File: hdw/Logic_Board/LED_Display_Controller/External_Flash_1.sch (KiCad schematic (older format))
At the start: 16 parts, among them U1801 SST25PF020B

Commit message: Added some digikey partnumbers to components
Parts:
- C1801: footprint (none) -> Capacitors_SMD:C_0603; Digi-Key PN PN -> 311-1344-1-ND; Voltage 25V -> 50V
- C1802: Digi-Key PN PN -> 1276-1921-1-ND; Voltage 25V -> 50V
- C1803: Digi-Key PN PN -> 1276-1018-1-ND; Voltage 25V -> 50V
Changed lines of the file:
@@
 F 0 "C1801" H 5815 5530 50  0000 L CNN
 F 1 "0.1uF" H 5815 5330 50  0000 L CNN
-F 2 "" H 5828 5280 50  0001 C CNN
+F 2 "Capacitors_SMD:C_0603" H 5828 5280 50  0001 C CNN
 F 3 "" H 5815 5530 50  0001 C CNN
 F 4 "0603" H 5640 5530 50  0000 R CNN "display_footprint"
-F 5 "25V" H 5640 5430 50  0000 R CNN "Voltage"
+F 5 "50V" H 5640 5430 50  0000 R CNN "Voltage"
 F 6 "X7R" H 5640 5330 50  0000 R CNN "Dielectric"
-F 7 "PN" H 6215 5930 60  0001 C CNN "Digi-Key PN"
+F 7 "311-1344-1-ND" H 6215 5930 60  0001 C CNN "Digi-Key PN"
 	1    5790 5430
 	1    0    0    -1
@@
 F 3 "" H 6115 5530 50  0001 C CNN
 F 4 "0603" H 5940 5530 50  0001 R CNN "display_footprint"
-F 5 "25V" H 5940 5430 50  0001 R CNN "Voltage"
+F 5 "50V" H 5940 5430 50  0001 R CNN "Voltage"
 F 6 "X7R" H 5940 5330 50  0001 R CNN "Dielectric"
-F 7 "PN" H 6515 5930 60  0001 C CNN "Digi-Key PN"
+F 7 "1276-1921-1-ND" H 6515 5930 60  0001 C CNN "Digi-Key PN"
 	1    6090 5430
 	1    0    0    -1
@@
 F 3 "" H 6415 5530 50  0001 C CNN
 F 4 "0603" H 6240 5530 50  0001 R CNN "display_footprint"
-F 5 "25V" H 6240 5430 50  0001 R CNN "Voltage"
+F 5 "50V" H 6240 5430 50  0001 R CNN "Voltage"
 F 6 "X7R" H 6240 5330 50  0001 R CNN "Dielectric"
-F 7 "PN" H 6815 5930 60  0001 C CNN "Digi-Key PN"
+F 7 "1276-1018-1-ND" H 6815 5930 60  0001 C CNN "Digi-Key PN"
 	1    6390 5430
 	1    0    0    -1

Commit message: Finished first pass of digikey part numbers
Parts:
- R1801, R1802, R1803, R1804, R1805, R1812: Digi-Key PN PN -> A106047CT-ND
- R1806, R1807, R1808, R1809, R1810, R1811: Digi-Key PN PN -> RMCF0603FT10K0CT-ND
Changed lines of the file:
@@
 F 5 "1%" H 5410 4320 50  0000 L CNN "Tolerance"
 F 6 "1/10W" H 5410 4240 50  0000 L CNN "Wattage"
-F 7 "PN" H 5630 4720 60  0001 C CNN "Digi-Key PN"
+F 7 "RMCF0603FT10K0CT-ND" H 5630 4720 60  0001 C CNN "Digi-Key PN"
 	1    5330 4320
 	1    0    0    -1
@@
 F 5 "1%" H 4600 4320 50  0000 L CNN "Tolerance"
 F 6 "1/10W" H 4600 4240 50  0000 L CNN "Wattage"
-F 7 "PN" H 4820 4720 60  0001 C CNN "Digi-Key PN"
+F 7 "RMCF0603FT10K0CT-ND" H 4820 4720 60  0001 C CNN "Digi-Key PN"
 	1    4520 4320
 	1    0    0    -1
@@
 F 5 "1%" H 5190 3130 50  0000 L CNN "Tolerance"
 F 6 "1/10W" H 5190 3050 50  0000 L CNN "Wattage"
-F 7 "PN" H 5410 3530 60  0001 C CNN "Digi-Key PN"
+F 7 "RMCF0603FT10K0CT-ND" H 5410 3530 60  0001 C CNN "Digi-Key PN"
 	1    5110 3130
 	1    0    0    -1
@@
 F 5 "1%" H 4600 3130 50  0000 L CNN "Tolerance"
 F 6 "1/10W" H 4600 3050 50  0000 L CNN "Wattage"
-F 7 "PN" H 4820 3530 60  0001 C CNN "Digi-Key PN"
+F 7 "RMCF0603FT10K0CT-ND" H 4820 3530 60  0001 C CNN "Digi-Key PN"
 	1    4520 3130
 	1    0    0    -1
@@
 F 5 "1%" H 4010 3130 50  0000 L CNN "Tolerance"
 F 6 "1/10W" H 4010 3050 50  0000 L CNN "Wattage"
-F 7 "PN" H 4230 3530 60  0001 C CNN "Digi-Key PN"
+F 7 "RMCF0603FT10K0CT-ND" H 4230 3530 60  0001 C CNN "Digi-Key PN"
 	1    3930 3130
 	1    0    0    -1
@@
 F 5 "1%" H 6830 3850 50  0000 L CNN "Tolerance"
 F 6 "1/10W" H 6830 3770 50  0000 L CNN "Wattage"
-F 7 "PN" H 7050 4250 60  0001 C CNN "Digi-Key PN"
+F 7 "RMCF0603FT10K0CT-ND" H 7050 4250 60  0001 C CNN "Digi-Key PN"
 	1    6750 3850
 	1    0    0    -1
@@
 F 5 "1%" V 3620 3450 50  0001 C CNN "Tolerance"
 F 6 "1/10W" V 3720 3450 50  0001 C CNN "Wattage"
-F 7 "PN" H 3720 3850 60  0001 C CNN "Digi-Key PN"
+F 7 "A106047CT-ND" H 3720 3850 60  0001 C CNN "Digi-Key PN"
 	1    3420 3450
 	0    1    1    0
@@
 F 5 "1%" V 7330 3450 50  0001 C CNN "Tolerance"
 F 6 "1/10W" V 7430 3450 50  0001 C CNN "Wattage"
-F 7 "PN" H 7430 3850 60  0001 C CNN "Digi-Key PN"
+F 7 "A106047CT-ND" H 7430 3850 60  0001 C CNN "Digi-Key PN"
 	1    7130 3450
 	0    1    1    0
@@
 F 5 "1%" V 3620 3550 50  0001 C CNN "Tolerance"
 F 6 "1/10W" V 3720 3550 50  0001 C CNN "Wattage"
-F 7 "PN" H 3720 3950 60  0001 C CNN "Digi-Key PN"
+F 7 "A106047CT-ND" H 3720 3950 60  0001 C CNN "Digi-Key PN"
 	1    3420 3550
 	0    1    1    0
@@
 F 5 "1%" V 3620 3750 50  0001 C CNN "Tolerance"
 F 6 "1/10W" V 3720 3750 50  0001 C CNN "Wattage"
-F 7 "PN" H 3720 4150 60  0001 C CNN "Digi-Key PN"
+F 7 "A106047CT-ND" H 3720 4150 60  0001 C CNN "Digi-Key PN"
 	1    3420 3750
 	0    1    1    0
@@
 F 5 "1%" V 3620 3850 50  0001 C CNN "Tolerance"
 F 6 "1/10W" V 3720 3850 50  0001 C CNN "Wattage"
-F 7 "PN" H 3720 4250 60  0001 C CNN "Digi-Key PN"
+F 7 "A106047CT-ND" H 3720 4250 60  0001 C CNN "Digi-Key PN"
 	1    3420 3850
 	0    1    1    0
@@
 F 5 "1%" V 3620 3650 50  0001 C CNN "Tolerance"
 F 6 "1/10W" V 3720 3650 50  0001 C CNN "Wattage"
-F 7 "PN" H 3720 4050 60  0001 C CNN "Digi-Key PN"
+F 7 "A106047CT-ND" H 3720 4050 60  0001 C CNN "Digi-Key PN"
 	1    3420 3650
 	0    1    1    0

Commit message: First pass assignment of footprints to all components
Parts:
- C1802, C1803: footprint (none) -> Capacitors_SMD:C_0603
- R1801, R1802, R1803, R1804, R1805, R1806, R1807, R1808, R1809, R1810, R1811, R1812: footprint (none) -> Resistors_SMD:R_0603
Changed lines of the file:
@@
 F 0 "R1810" H 5270 4320 50  0000 R CNN
 F 1 "10k" V 5330 4320 50  0000 C CNN
-F 2 "" H 5330 4320 50  0001 C CNN
+F 2 "Resistors_SMD:R_0603" H 5330 4320 50  0001 C CNN
 F 3 "" H 5330 4320 50  0001 C CNN
 F 4 "0603" H 5410 4400 50  0000 L CNN "display_footprint"
@@
 F 0 "R1808" H 4460 4320 50  0000 R CNN
 F 1 "10k" V 4520 4320 50  0000 C CNN
-F 2 "" H 4520 4320 50  0001 C CNN
+F 2 "Resistors_SMD:R_0603" H 4520 4320 50  0001 C CNN
 F 3 "" H 4520 4320 50  0001 C CNN
 F 4 "0603" H 4600 4400 50  0000 L CNN "display_footprint"
@@
 F 0 "R1809" H 5050 3130 50  0000 R CNN
 F 1 "10k" V 5110 3130 50  0000 C CNN
-F 2 "" H 5110 3130 50  0001 C CNN
+F 2 "Resistors_SMD:R_0603" H 5110 3130 50  0001 C CNN
 F 3 "" H 5110 3130 50  0001 C CNN
 F 4 "0603" H 5190 3210 50  0000 L CNN "display_footprint"
@@
 F 0 "R1807" H 4460 3130 50  0000 R CNN
 F 1 "10k" V 4520 3130 50  0000 C CNN
-F 2 "" H 4520 3130 50  0001 C CNN
+F 2 "Resistors_SMD:R_0603" H 4520 3130 50  0001 C CNN
 F 3 "" H 4520 3130 50  0001 C CNN
 F 4 "0603" H 4600 3210 50  0000 L CNN "display_footprint"
@@
 F 0 "R1806" H 3870 3130 50  0000 R CNN
 F 1 "10k" V 3930 3130 50  0000 C CNN
-F 2 "" H 3930 3130 50  0001 C CNN
+F 2 "Resistors_SMD:R_0603" H 3930 3130 50  0001 C CNN
 F 3 "" H 3930 3130 50  0001 C CNN
 F 4 "0603" H 4010 3210 50  0000 L CNN "display_footprint"
@@
 F 0 "R1811" H 6690 3850 50  0000 R CNN
 F 1 "10k" V 6750 3850 50  0000 C CNN
-F 2 "" H 6750 3850 50  0001 C CNN
+F 2 "Resistors_SMD:R_0603" H 6750 3850 50  0001 C CNN
 F 3 "" H 6750 3850 50  0001 C CNN
 F 4 "0603" H 6830 3930 50  0000 L CNN "display_footprint"
@@
 F 0 "R1801" V 3380 3580 50  0000 L CNN
 F 1 "100" V 3420 3450 50  0000 C CNN
-F 2 "" H 3420 3450 50  0001 C CNN
+F 2 "Resistors_SMD:R_0603" H 3420 3450 50  0001 C CNN
 F 3 "" H 3420 3450 50  0001 C CNN
 F 4 "0603" V 3520 3450 50  0001 C CNN "display_footprint"
@@
 F 0 "R1812" V 7030 3450 50  0000 C CNN
 F 1 "100" V 7130 3450 50  0000 C CNN
-F 2 "" H 7130 3450 50  0001 C CNN
+F 2 "Resistors_SMD:R_0603" H 7130 3450 50  0001 C CNN
 F 3 "" H 7130 3450 50  0001 C CNN
 F 4 "0603" V 7230 3450 50  0001 C CNN "display_footprint"
@@
 F 0 "C1802" H 6115 5530 50  0000 L CNN
 F 1 "10nF" H 6115 5330 50  0000 L CNN
-F 2 "" H 6128 5280 50  0001 C CNN
+F 2 "Capacitors_SMD:C_0603" H 6128 5280 50  0001 C CNN
 F 3 "" H 6115 5530 50  0001 C CNN
 F 4 "0603" H 5940 5530 50  0001 R CNN "display_footprint"
@@
 F 0 "C1803" H 6415 5530 50  0000 L CNN
 F 1 "1nF" H 6415 5330 50  0000 L CNN
-F 2 "" H 6428 5280 50  0001 C CNN
+F 2 "Capacitors_SMD:C_0603" H 6428 5280 50  0001 C CNN
 F 3 "" H 6415 5530 50  0001 C CNN
 F 4 "0603" H 6240 5530 50  0001 R CNN "display_footprint"
@@
 F 0 "R1802" V 3380 3680 50  0000 L CNN
 F 1 "100" V 3420 3550 50  0000 C CNN
-F 2 "" H 3420 3550 50  0001 C CNN
+F 2 "Resistors_SMD:R_0603" H 3420 3550 50  0001 C CNN
 F 3 "" H 3420 3550 50  0001 C CNN
 F 4 "0603" V 3520 3550 50  0001 C CNN "display_footprint"
@@
 F 0 "R1804" V 3380 3880 50  0000 L CNN
 F 1 "100" V 3420 3750 50  0000 C CNN
-F 2 "" H 3420 3750 50  0001 C CNN
+F 2 "Resistors_SMD:R_0603" H 3420 3750 50  0001 C CNN
 F 3 "" H 3420 3750 50  0001 C CNN
 F 4 "0603" V 3520 3750 50  0001 C CNN "display_footprint"
@@
 F 0 "R1805" V 3380 3980 50  0000 L CNN
 F 1 "100" V 3420 3850 50  0000 C CNN
-F 2 "" H 3420 3850 50  0001 C CNN
+F 2 "Resistors_SMD:R_0603" H 3420 3850 50  0001 C CNN
 F 3 "" H 3420 3850 50  0001 C CNN
 F 4 "0603" V 3520 3850 50  0001 C CNN "display_footprint"
@@
 F 0 "R1803" V 3380 3780 50  0000 L CNN
 F 1 "100" V 3420 3650 50  0000 C CNN
-F 2 "" H 3420 3650 50  0001 C CNN
+F 2 "Resistors_SMD:R_0603" H 3420 3650 50  0001 C CNN
 F 3 "" H 3420 3650 50  0001 C CNN
 F 4 "0603" V 3520 3650 50  0001 C CNN "display_footprint"

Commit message: Resolved a few library dependencies
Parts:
- R1801, R1802, R1803, R1804, R1805, R1806, R1807, R1808, R1809, R1810, R1811, R1812: symbol Custom_Library:R_Custom -> LED_Display_Local_Library:R_Custom
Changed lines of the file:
@@
 $EndComp
 $Comp
-L Custom_Library:R_Custom R1810
+L LED_Display_Local_Library:R_Custom R1810
 U 1 1 5BB4E3FC
 P 5330 4320
@@
 $EndComp
 $Comp
-L Custom_Library:R_Custom R1808
+L LED_Display_Local_Library:R_Custom R1808
 U 1 1 5BB4EACF
 P 4520 4320
@@
 $EndComp
 $Comp
-L Custom_Library:R_Custom R1809
+L LED_Display_Local_Library:R_Custom R1809
 U 1 1 5BB4EB13
 P 5110 3130
@@
 $EndComp
 $Comp
-L Custom_Library:R_Custom R1807
+L LED_Display_Local_Library:R_Custom R1807
 U 1 1 5BB4EB5D
 P 4520 3130
@@
 $EndComp
 $Comp
-L Custom_Library:R_Custom R1806
+L LED_Display_Local_Library:R_Custom R1806
 U 1 1 5BB4EBA3
 P 3930 3130
@@
 $EndComp
 $Comp
-L Custom_Library:R_Custom R1811
+L LED_Display_Local_Library:R_Custom R1811
 U 1 1 5BB4EDD1
 P 6750 3850
@@
 $EndComp
 $Comp
-L Custom_Library:R_Custom R1801
+L LED_Display_Local_Library:R_Custom R1801
 U 1 1 5BB4F53B
 P 3420 3450
@@
 Connection ~ 3930 3650
 $Comp
-L Custom_Library:R_Custom R1812
+L LED_Display_Local_Library:R_Custom R1812
 U 1 1 5BB511F8
 P 7130 3450
@@
 	6090 5240 6390 5240
 $Comp
-L Custom_Library:R_Custom R1802
+L LED_Display_Local_Library:R_Custom R1802
 U 1 1 5BBE5753
 P 3420 3550
@@
 $EndComp
 $Comp
-L Custom_Library:R_Custom R1804
+L LED_Display_Local_Library:R_Custom R1804
 U 1 1 5BBE5DA1
 P 3420 3750
@@
 $EndComp
 $Comp
-L Custom_Library:R_Custom R1805
+L LED_Display_Local_Library:R_Custom R1805
 U 1 1 5BBE5DFB
 P 3420 3850
@@
 FLASH_MOSI
 $Comp
-L Custom_Library:R_Custom R1803
+L LED_Display_Local_Library:R_Custom R1803
 U 1 1 5BC1B439
 P 3420 3650

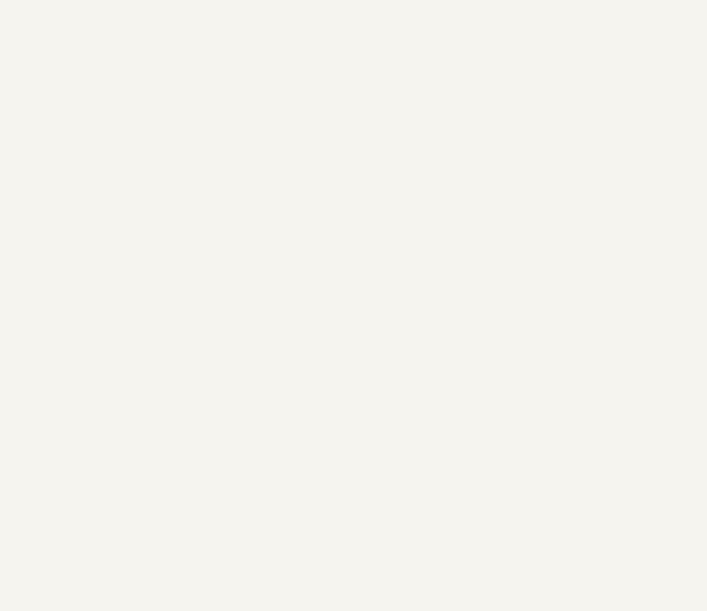
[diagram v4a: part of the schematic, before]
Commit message: Added flash chip select LEDs
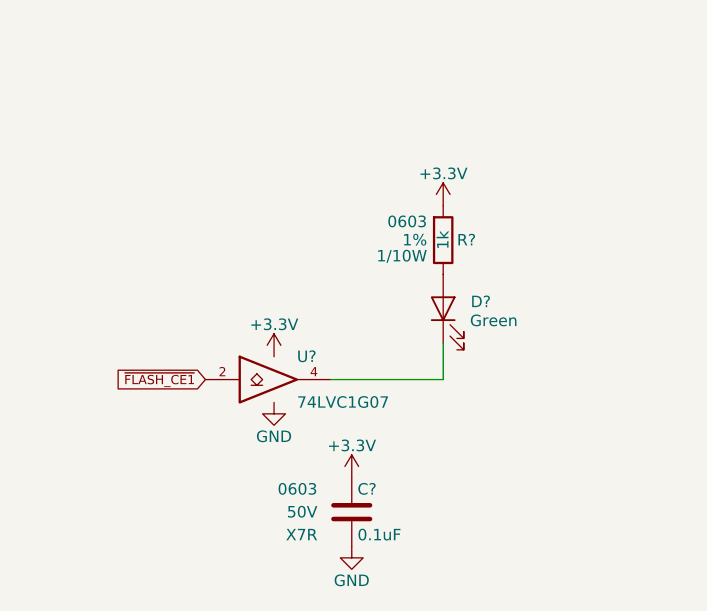
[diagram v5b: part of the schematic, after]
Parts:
- added C?: 0.1uF, Capacitors_SMD:C_0603, symbol LED_Display_Local_Library:C_Custom
- added D?: Green, LEDs:LED_0603, symbol Device:LED
- added R?: 1k, Resistors_SMD:R_0603, symbol LED_Display_Local_Library:R_Custom
- added U?: 74LVC1G07, TO_SOT_Packages_SMD:SOT-353_SC-70-5, symbol LED_Display_Local_Library:74LVC1G07_Power
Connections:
- net +3V3: now also C?.1, R?.1, U?.5 (VCC)
- net GND: now also C?.2, U?.3 (GND)
- net ~FLASH_CE1: now also U?.2
- new net: D?.1 (K), U?.4
- new net: D?.2 (A), R?.2
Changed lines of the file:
@@
 Wire Wire Line
 	4520 3850 5680 3850
+$Comp
+L LED_Display_Local_Library:C_Custom C?
+U 1 1 5C15F697
+P 2010 6900
+AR Path="/5BAAE16C/5C15F697" Ref="C?"  Part="1"
+AR Path="/5BB181D8/5C15F697" Ref="C?"  Part="1"
+AR Path="/5BB2595E/5C15F697" Ref="C?"  Part="1"
+F 0 "C?" H 2035 7000 50  0000 L CNN
+F 1 "0.1uF" H 2035 6800 50  0000 L CNN
+F 2 "Capacitors_SMD:C_0603" H 2048 6750 50  0001 C CNN
+F 3 "" H 2035 7000 50  0001 C CNN
+F 4 "0603" H 1860 7000 50  0000 R CNN "display_footprint"
+F 5 "50V" H 1860 6900 50  0000 R CNN "Voltage"
+F 6 "X7R" H 1860 6800 50  0000 R CNN "Dielectric"
+F 7 "311-1344-1-ND" H 2435 7400 60  0001 C CNN "Digi-Key PN"
+	1    2010 6900
+	1    0    0    -1
+$EndComp
+$Comp
+L LED_Display_Local_Library:74LVC1G07_Power U?
+U 1 1 5C161AE1
+P 1670 6320
+F 0 "U?" H 1770 6420 50  0000 L CNN
+F 1 "74LVC1G07" H 1770 6220 50  0000 L CNN
+F 2 "TO_SOT_Packages_SMD:SOT-353_SC-70-5" H 1670 6320 50  0001 C CNN
+F 3 "http://www.ti.com/lit/sg/scyt129e/scyt129e.pdf" H 1670 6320 50  0001 C CNN
+F 4 "296-8486-1-ND" H 1670 6320 50  0001 C CNN "Digi-Key PN"
+	1    1670 6320
+	1    0    0    -1
+$EndComp
+$Comp
+L power:+3.3V #PWR?
+U 1 1 5C161B83
+P 1670 6220
+F 0 "#PWR?" H 1670 6070 50  0001 C CNN
+F 1 "+3.3V" H 1670 6360 50  0000 C CNN
+F 2 "" H 1670 6220 50  0001 C CNN
+F 3 "" H 1670 6220 50  0001 C CNN
+	1    1670 6220
+	1    0    0    -1
+$EndComp
+$Comp
+L power:+3.3V #PWR?
+U 1 1 5C161BE9
+P 2010 6750
+F 0 "#PWR?" H 2010 6600 50  0001 C CNN
+F 1 "+3.3V" H 2010 6890 50  0000 C CNN
+F 2 "" H 2010 6750 50  0001 C CNN
+F 3 "" H 2010 6750 50  0001 C CNN
+	1    2010 6750
+	1    0    0    -1
+$EndComp
+$Comp
+L power:GND #PWR?
+U 1 1 5C161C44
+P 2010 7050
+F 0 "#PWR?" H 2010 6800 50  0001 C CNN
+F 1 "GND" H 2010 6900 50  0000 C CNN
+F 2 "" H 2010 7050 50  0001 C CNN
+F 3 "" H 2010 7050 50  0001 C CNN
+	1    2010 7050
+	1    0    0    -1
+$EndComp
+$Comp
+L power:GND #PWR?
+U 1 1 5C161C9F
+P 1670 6420
+F 0 "#PWR?" H 1670 6170 50  0001 C CNN
+F 1 "GND" H 1670 6270 50  0000 C CNN
+F 2 "" H 1670 6420 50  0001 C CNN
+F 3 "" H 1670 6420 50  0001 C CNN
+	1    1670 6420
+	1    0    0    -1
+$EndComp
+Text GLabel 1370 6320 0    40   Input ~ 0
+~FLASH_CE1
+$Comp
+L power:+3.3V #PWR?
+U 1 1 5C166A81
+P 2410 5560
+AR Path="/5BB844FD/5C166A81" Ref="#PWR?"  Part="1"
+AR Path="/5BF346B3/5C166A81" Ref="#PWR?"  Part="1"
+AR Path="/5BB2595E/5C166A81" Ref="#PWR?"  Part="1"
+F 0 "#PWR?" H 2410 5410 50  0001 C CNN
+F 1 "+3.3V" H 2410 5700 50  0000 C CNN
+F 2 "" H 2410 5560 50  0001 C CNN
+F 3 "" H 2410 5560 50  0001 C CNN
+	1    2410 5560
+	1    0    0    -1
+$EndComp
+Wire Wire Line
+	1920 6320 2410 6320
+Wire Wire Line
+	2410 6320 2410 6160
+$Comp
+L LED_Display_Local_Library:R_Custom R?
+U 1 1 5C166A8D
+P 2410 5710
+AR Path="/5BAAE1F3/5C166A8D" Ref="R?"  Part="1"
+AR Path="/5BAAE1DC/5C166A8D" Ref="R?"  Part="1"
+AR Path="/5BAAE16C/5C166A8D" Ref="R?"  Part="1"
+AR Path="/5BB844FD/5C166A8D" Ref="R?"  Part="1"
+AR Path="/5BF346B3/5C166A8D" Ref="R?"  Part="1"
+AR Path="/5BB2595E/5C166A8D" Ref="R?"  Part="1"
+F 0 "R?" H 2350 5710 50  0000 R CNN
+F 1 "1k" V 2410 5710 50  0000 C CNN
+F 2 "Resistors_SMD:R_0603" H 2410 5710 50  0001 C CNN
+F 3 "" H 2410 5710 50  0001 C CNN
+F 4 "0603" H 2480 5790 50  0000 L CNN "display_footprint"
+F 5 "1%" H 2480 5710 50  0000 L CNN "Tolerance"
+F 6 "1/10W" H 2480 5640 50  0000 L CNN "Wattage"
+F 7 "RMCF0603FT1K00CT-ND" H 2710 6110 60  0001 C CNN "Digi-Key PN"
+	1    2410 5710
+	-1   0    0    -1
+$EndComp
+$Comp
+L Device:LED D?
+U 1 1 5C166A95
+P 2410 6010
+AR Path="/5BB844FD/5C166A95" Ref="D?"  Part="1"
+AR Path="/5BF346B3/5C166A95" Ref="D?"  Part="1"
+AR Path="/5BB2595E/5C166A95" Ref="D?"  Part="1"
+F 0 "D?" V 2440 5890 50  0000 R CNN
+F 1 "Green" V 2357 5893 50  0000 R CNN
+F 2 "LEDs:LED_0603" H 2410 6010 50  0001 C CNN
+F 3 "~" H 2410 6010 50  0001 C CNN
+F 4 "160-1446-1-ND" H -2600 3010 50  0001 C CNN "Digi-Key PN"
+	1    2410 6010
+	0    -1   -1   0
+$EndComp
 $EndSCHEMATC

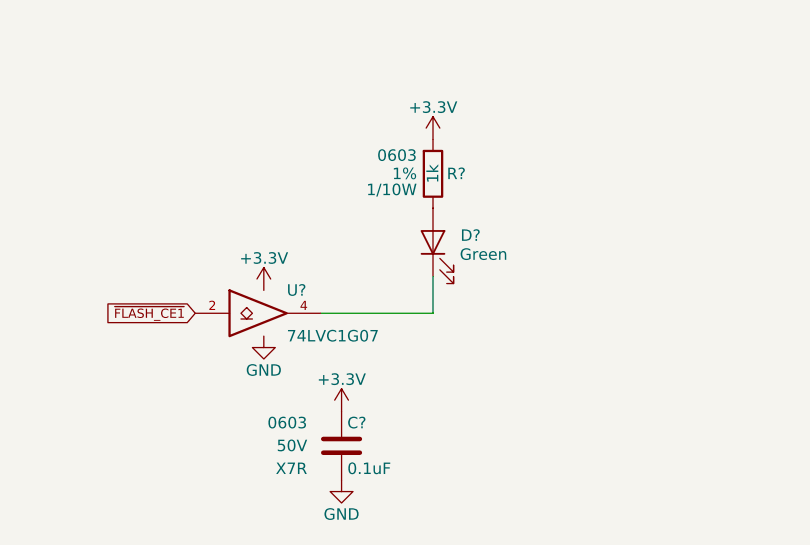
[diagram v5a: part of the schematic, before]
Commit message: Added WIFI comm LED
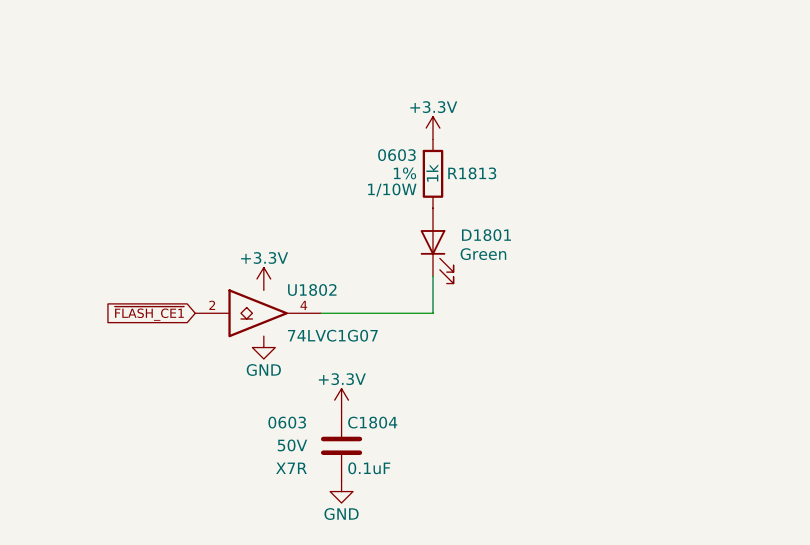
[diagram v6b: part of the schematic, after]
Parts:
- gave numbers to parts that had none: 4
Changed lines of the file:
@@
 AR Path="/5BAAE16C/5C15F697" Ref="C?"  Part="1"
 AR Path="/5BB181D8/5C15F697" Ref="C?"  Part="1"
-AR Path="/5BB2595E/5C15F697" Ref="C?"  Part="1"
-F 0 "C?" H 2035 7000 50  0000 L CNN
+AR Path="/5BB2595E/5C15F697" Ref="C1804"  Part="1"
+F 0 "C1804" H 2035 7000 50  0000 L CNN
 F 1 "0.1uF" H 2035 6800 50  0000 L CNN
 F 2 "Capacitors_SMD:C_0603" H 2048 6750 50  0001 C CNN
@@
 $EndComp
 $Comp
-L LED_Display_Local_Library:74LVC1G07_Power U?
+L LED_Display_Local_Library:74LVC1G07_Power U1802
 U 1 1 5C161AE1
 P 1670 6320
-F 0 "U?" H 1770 6420 50  0000 L CNN
+F 0 "U1802" H 1770 6420 50  0000 L CNN
 F 1 "74LVC1G07" H 1770 6220 50  0000 L CNN
 F 2 "TO_SOT_Packages_SMD:SOT-353_SC-70-5" H 1670 6320 50  0001 C CNN
@@
 $EndComp
 $Comp
-L power:+3.3V #PWR?
+L power:+3.3V #PWR01811
 U 1 1 5C161B83
 P 1670 6220
-F 0 "#PWR?" H 1670 6070 50  0001 C CNN
+F 0 "#PWR01811" H 1670 6070 50  0001 C CNN
 F 1 "+3.3V" H 1670 6360 50  0000 C CNN
 F 2 "" H 1670 6220 50  0001 C CNN
@@
 $EndComp
 $Comp
-L power:+3.3V #PWR?
+L power:+3.3V #PWR01813
 U 1 1 5C161BE9
 P 2010 6750
-F 0 "#PWR?" H 2010 6600 50  0001 C CNN
+F 0 "#PWR01813" H 2010 6600 50  0001 C CNN
 F 1 "+3.3V" H 2010 6890 50  0000 C CNN
 F 2 "" H 2010 6750 50  0001 C CNN
@@
 $EndComp
 $Comp
-L power:GND #PWR?
+L power:GND #PWR01814
 U 1 1 5C161C44
 P 2010 7050
-F 0 "#PWR?" H 2010 6800 50  0001 C CNN
+F 0 "#PWR01814" H 2010 6800 50  0001 C CNN
 F 1 "GND" H 2010 6900 50  0000 C CNN
 F 2 "" H 2010 7050 50  0001 C CNN
@@
 $EndComp
 $Comp
-L power:GND #PWR?
+L power:GND #PWR01812
 U 1 1 5C161C9F
 P 1670 6420
-F 0 "#PWR?" H 1670 6170 50  0001 C CNN
+F 0 "#PWR01812" H 1670 6170 50  0001 C CNN
 F 1 "GND" H 1670 6270 50  0000 C CNN
 F 2 "" H 1670 6420 50  0001 C CNN
@@
 AR Path="/5BB844FD/5C166A81" Ref="#PWR?"  Part="1"
 AR Path="/5BF346B3/5C166A81" Ref="#PWR?"  Part="1"
-AR Path="/5BB2595E/5C166A81" Ref="#PWR?"  Part="1"
-F 0 "#PWR?" H 2410 5410 50  0001 C CNN
+AR Path="/5BB2595E/5C166A81" Ref="#PWR01815"  Part="1"
+F 0 "#PWR01815" H 2410 5410 50  0001 C CNN
 F 1 "+3.3V" H 2410 5700 50  0000 C CNN
 F 2 "" H 2410 5560 50  0001 C CNN
@@
 AR Path="/5BB844FD/5C166A8D" Ref="R?"  Part="1"
 AR Path="/5BF346B3/5C166A8D" Ref="R?"  Part="1"
-AR Path="/5BB2595E/5C166A8D" Ref="R?"  Part="1"
-F 0 "R?" H 2350 5710 50  0000 R CNN
+AR Path="/5BB2595E/5C166A8D" Ref="R1813"  Part="1"
+F 0 "R1813" H 2350 5710 50  0000 R CNN
 F 1 "1k" V 2410 5710 50  0000 C CNN
 F 2 "Resistors_SMD:R_0603" H 2410 5710 50  0001 C CNN
@@
 AR Path="/5BB844FD/5C166A95" Ref="D?"  Part="1"
 AR Path="/5BF346B3/5C166A95" Ref="D?"  Part="1"
-AR Path="/5BB2595E/5C166A95" Ref="D?"  Part="1"
-F 0 "D?" V 2440 5890 50  0000 R CNN
+AR Path="/5BB2595E/5C166A95" Ref="D1801"  Part="1"
+F 0 "D1801" V 2440 5890 50  0000 R CNN
 F 1 "Green" V 2357 5893 50  0000 R CNN
 F 2 "LEDs:LED_0603" H 2410 6010 50  0001 C CNN
